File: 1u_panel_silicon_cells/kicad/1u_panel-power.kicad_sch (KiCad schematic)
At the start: 66 parts, among them J1 MMS-104-01-[F/L]-SH, Q1 DMP3050LVT-7, Q2 DMP2240UDM-7, U10 TPS63060DSCR, U12 LTC4412, U3 LT1618EMSTRPBF, U4 INA226AIDGSR

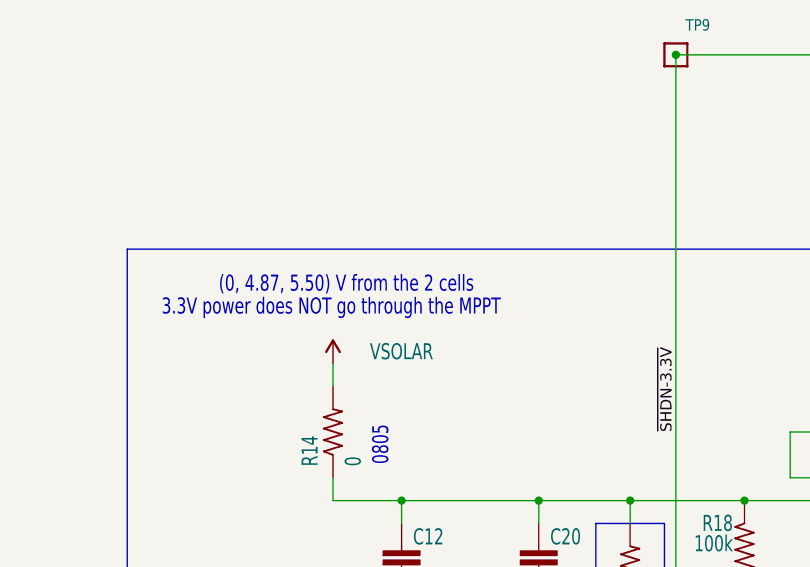
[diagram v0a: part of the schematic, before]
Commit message: fixed board outline, title blocks
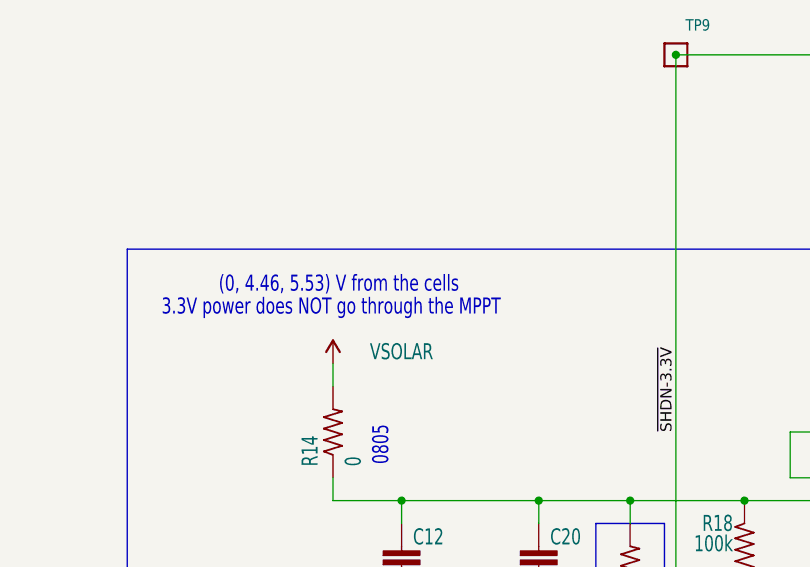
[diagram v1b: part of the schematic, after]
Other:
- note added: "(0, 4.46, 5.53) V from the cells"
- note removed: "(0, 4.87, 5.50) V from the 2 cells"
- title: OreSat Solar Module (for Frame 2.0) -> OreSat Silicon Solar Module (for Frame 2.0)
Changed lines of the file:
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@@
 	(paper "USLedger")
 	(title_block
-		(title "OreSat Solar Module (for Frame 2.0)")
-		(date "2023-12-20")
-		(rev "6.0")
+		(title "OreSat Silicon Solar Module (for Frame 2.0)")
+		(date "2024-08-18")
+		(rev "1.0")
 	)
 	(junction
@@
 		)
 	)
-	(text "(0, 4.87, 5.50) V from the 2 cells"
+	(text "(0, 4.46, 5.53) V from the cells"
 		(exclude_from_sim no)
 		(at 116.84 167.64 0)

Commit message: updating remote repo for design review
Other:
- moved on the sheet: C14
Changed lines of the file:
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@@
 	(wire
 		(pts
-			(xy 162.56 69.85) (xy 162.56 67.31)
+			(xy 162.56 69.85) (xy 162.56 68.58)
 		)
 		(stroke
@@
 	(wire
 		(pts
+			(xy 162.56 60.96) (xy 162.56 59.69)
+		)
+		(stroke
+			(width 0)
+			(type default)
+		)
+	)
+	(wire
+		(pts
 			(xy 91.44 90.17) (xy 93.98 90.17)
 		)
@@
 	(symbol
 		(lib_id "1u_panel-eagle-import:oresat-rcl_C-EU0603-C-NOSILK")
-		(at 162.56 62.23 0)
+		(at 162.56 63.5 0)
 		(unit 1)
 		(exclude_from_sim no)
@@
 		(dnp no)
 		(property "Reference" "C14"
-			(at 164.084 61.849 0)
+			(at 164.084 63.119 0)
 			(effects
 				(font
@@
 		)
 		(property "Value" "4.7u"
-			(at 164.084 66.929 0)
+			(at 164.084 68.199 0)
 			(effects
 				(font
@@
 		)
 		(property "Footprint" "1u_panel:.0603-C-NOSILK"
-			(at 162.56 62.23 0)
+			(at 162.56 63.5 0)
 			(effects
 				(font
@@
 		)
 		(property "Datasheet" ""
-			(at 162.56 62.23 0)
+			(at 162.56 63.5 0)
 			(effects
 				(font
@@
 		)
 		(property "Description" ""
-			(at 162.56 62.23 0)
+			(at 162.56 63.5 0)
 			(effects
 				(font
@@
 		)
 		(property "DIS" "Digi-Key"
-			(at 162.56 62.23 0)
+			(at 162.56 63.5 0)
 			(effects
 				(font
@@
 		)
 		(property "DPN" "587-4332-1-ND"
-			(at 162.56 62.23 0)
+			(at 162.56 63.5 0)
 			(effects
 				(font
@@
 		)
 		(property "MFR" "Taiyo"
-			(at 162.56 62.23 0)
+			(at 162.56 63.5 0)
 			(effects
 				(font
@@
 		)
 		(property "MPN" "EMK107BBJ475KAHT"
-			(at 162.56 62.23 0)
+			(at 162.56 63.5 0)
 			(effects
 				(font

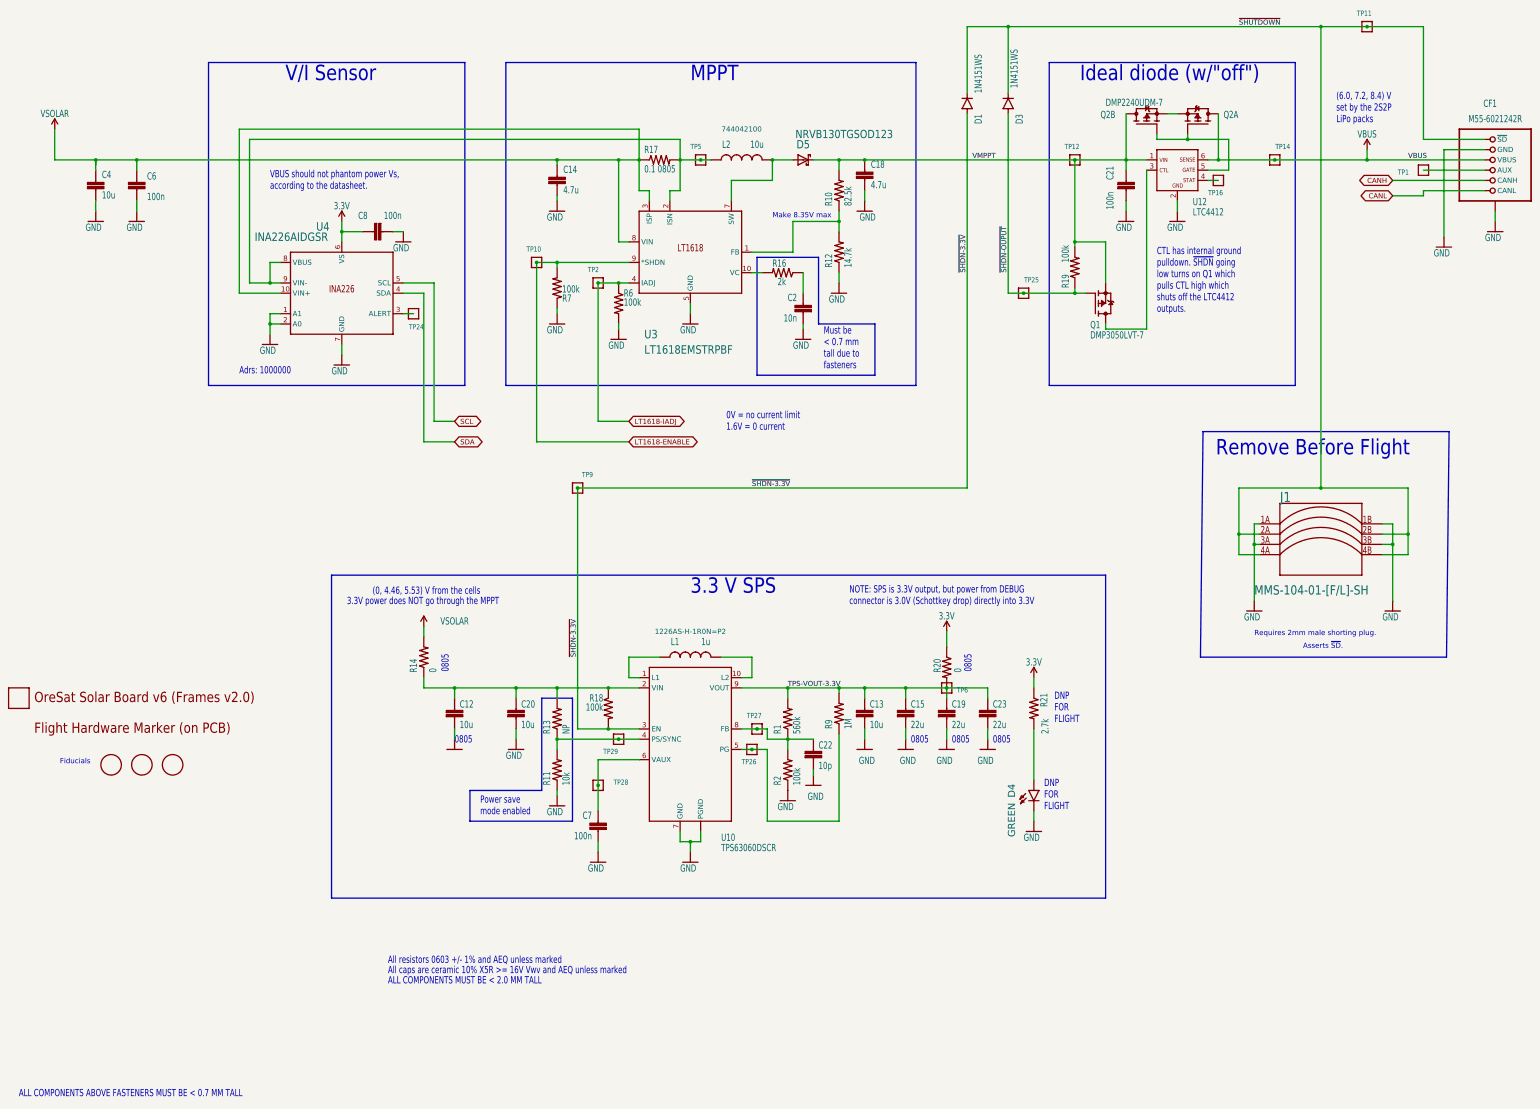
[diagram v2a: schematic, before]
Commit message: commiting silicon solar panel before moving programming header
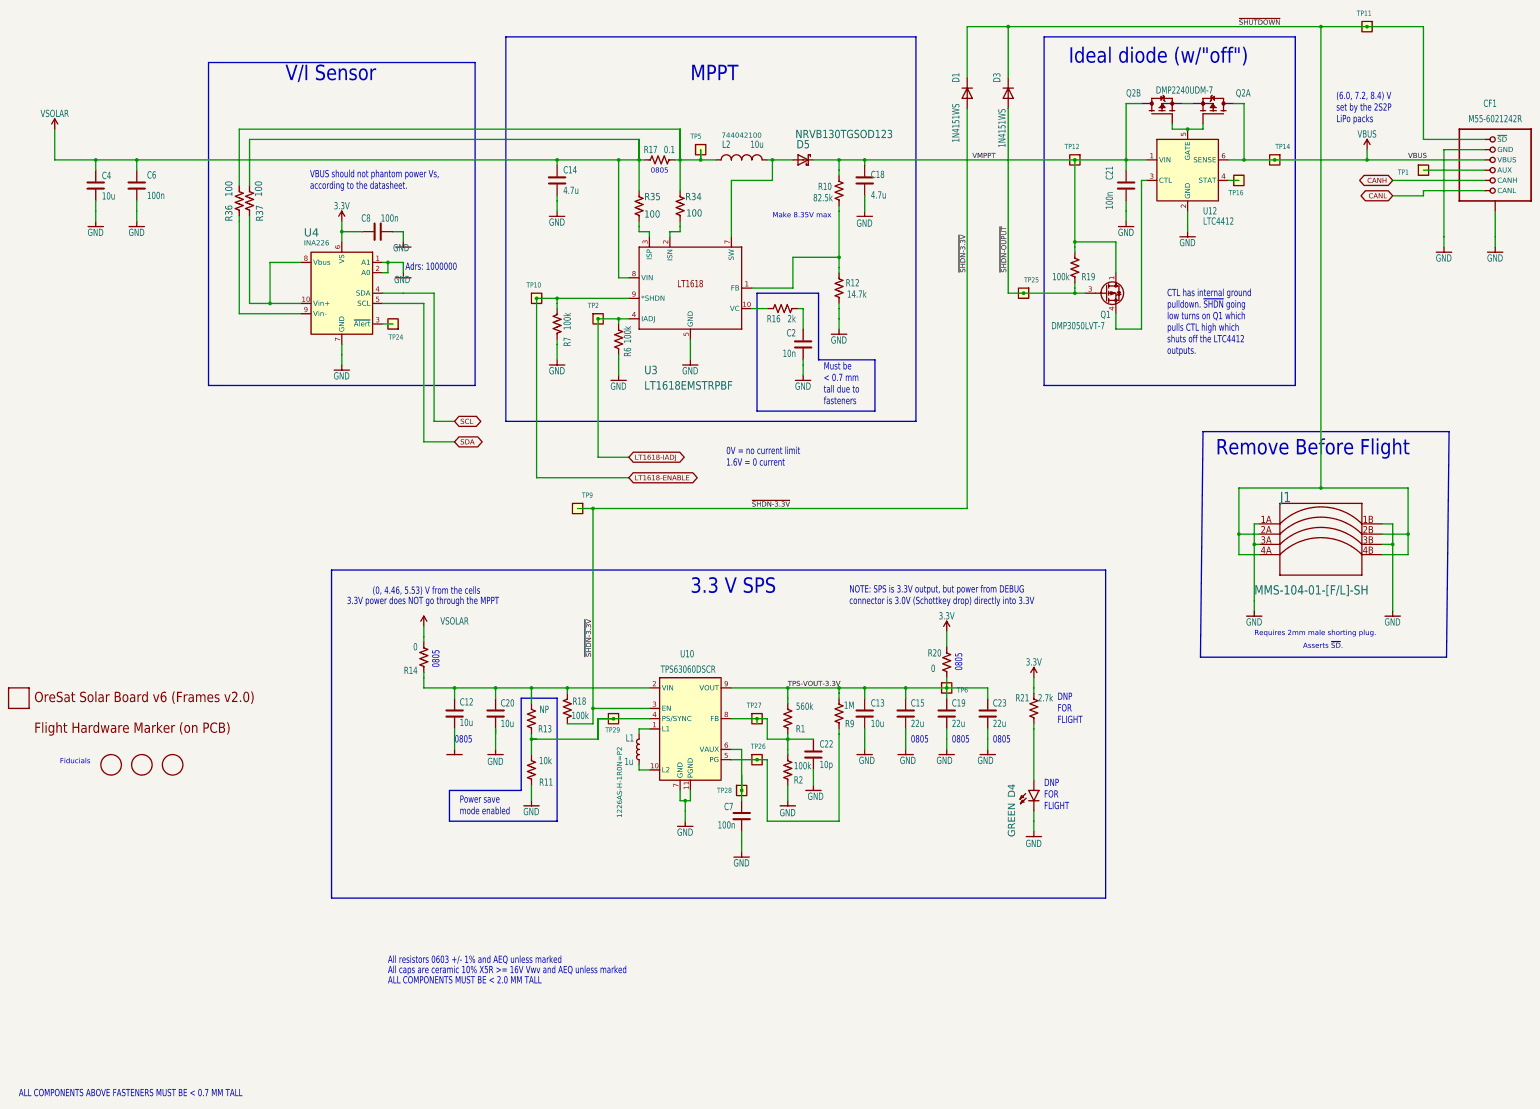
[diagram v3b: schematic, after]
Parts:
- removed U4: INA226AIDGSR, 1u_panel:DGS10, symbol 1u_panel-eagle-import:INA226AIDGSR
- added R34, R35, R36, R37: 100, oresat-passives:0603-C-NOSILK, symbol Device:R_US
- added U4: INA226, Package_SO:VSSOP-10_3x3mm_P0.5mm, symbol Sensor_Energy:INA226
- C12: footprint 1u_panel:.0805-B-NOSILK -> oresat-passives:0805-C-NOSILK; symbol 1u_panel-eagle-import:oresat-rcl_C-EU0805-B-NOSILK -> Device:C; DPN 490-12379-2-ND -> 490-12379-1-ND
- C13, C14, C18, C2, C20, C22, C4, C6, C7, C8: footprint 1u_panel:.0603-C-NOSILK -> oresat-passives:0603-C-NOSILK; symbol 1u_panel-eagle-import:oresat-rcl_C-EU0603-C-NOSILK -> Device:C
- C15, C19, C23: footprint 1u_panel:.0805-B-NOSILK -> oresat-passives:0805-C-NOSILK; symbol 1u_panel-eagle-import:oresat-rcl_C-EU0805-B-NOSILK -> Device:C; DPN 1276-6817-1-ND -> 2571-GMC21X7R226M10NTTR-ND; MFR Samsung -> Cal-Chip; MPN CL32B226KOJVPNE -> GMC21X7R226M10NT
- C21: footprint 1u_panel:.0402-B-NOSILK -> oresat-passives:0603-C-NOSILK; symbol 1u_panel-eagle-import:C-EU0402-B-NOSILK -> Device:C
- CF1: footprint 1u_panel:HARWIN-M55-60X1242R -> oresat-connectors:J-Harwin-M55-60X1242R; symbol 1u_panel-eagle-import:SOLAR-BOARD-CONNECTOR -> oresat-connectors:M55-6021242R; DIS (none) -> Digi-Key; DPN (none) -> 952-3851-2-ND; MFR (none) -> Harwin; MPN (none) -> M55-6021242R
- D1, D3: footprint 1u_panel:SOD323-R -> oresat-diodes:D-SOD323-R; symbol 1u_panel-eagle-import:DIODE-SOD323-R -> Device:D; DIS (none) -> Digi-Key; DPN (none) -> 12-1N4151WS-E3-08TR-ND; MFR (none) -> Vishay; MPN (none) -> 1N4151WS-E3-08
- D4: footprint 1u_panel:LED-0603 -> oresat-diodes:LED-0603
- D5: footprint 1u_panel:SOD123 -> oresat-diodes:SOD123
- J1: footprint 1u_panel:SAMTEC-MMS-104-02-X-SH -> oresat-connectors:SAMTEC-MMS-104-02-X-SH; symbol 1u_panel-eagle-import:SAMTEC-MMS-104-02-X-SHJ -> oresat-connectors:SAMTEC-MMS-104-02-X-SHJ; DIS (none) -> Digi-Key; DPN (none) -> SAM1237-04-ND; MFR (none) -> Samtec; MPN (none) -> MMS-104-02-L-SH
- L1: footprint 1u_panel:IND_1226AS-H-1R0N=P2 -> oresat-passives:IND_1226AS-H-1R0N=P2; symbol 1u_panel-eagle-import:L-MURATA-1226AS-H-1R0N=P2 -> Device:L
- L2: footprint 1u_panel:NONSTANDARD -> oresat-passives:744042100; symbol 1u_panel-eagle-import:L-WURTH-744042100 -> oresat-passives:L_BIG
- PCB1: value ORESAT-SOLAR-BOARD-V4-SPECTROLABS -> ORESAT-SOLAR-BOARD-V1.0-SILICON-CELLS; footprint 1u_panel:ORESAT-SOLAR-BOARD-V4 -> oresat-pcbs:ORESAT-SOLAR-BOARD-V4; MFR (none) -> ORESAT BABAAAYYYYY
- Q1: footprint 1u_panel:SOT23-6 -> Package_TO_SOT_SMD:SOT-23-6; symbol 1u_panel-eagle-import:MOSFET-PCH-SOT23-6 -> oresat-transistors:DMP3050LVT-7
- Q2: footprint 1u_panel:SOT23-6 -> Package_TO_SOT_SMD:SOT-23-6; symbol 1u_panel-eagle-import:Q-MOSFET-PCH-dual-SOT23-6_MOSFET-PCH-SOT23-6 -> oresat-transistors:DMP2240UDM-7
- R1, R10, R13, R16, R18, R19, R2, R21, R6, R7: footprint 1u_panel:.0603-C-NOSILK -> oresat-passives:0603-C-NOSILK; symbol 1u_panel-eagle-import:R-US_0603-C-NOSILK -> Device:R_US
- R11: footprint 1u_panel:.0603-C-NOSILK -> oresat-passives:0603-C-NOSILK; symbol 1u_panel-eagle-import:R-US_0603-C-NOSILK -> Device:R_US; DIS (none) -> Digi-Key; DPN (none) -> RMCF0603JT10K0; MFR (none) -> Stackpole; MPN (none) -> RMCF0603JT10K0
- R12: footprint 1u_panel:.0603-C-NOSILK -> oresat-passives:0603-C-NOSILK; symbol 1u_panel-eagle-import:R-US_0603-C-NOSILK -> Device:R_US; DPN 2019-RN73R1JTTD1422D25CT-ND -> RMCF0603FT14K7TR-ND; MFR KOA -> Stackpole; MPN RN73R1JTTD1422D25 -> RMCF0603FT14K7
- R14, R20: footprint 1u_panel:.0805-C-NOSILK -> oresat-passives:0805-C-NOSILK; symbol 1u_panel-eagle-import:R-US_0805-C-NOSILK -> Device:R_US
- R17: value 0.1 0805 -> 0.1; footprint 1u_panel:.0805-C-NOSILK -> oresat-passives:0805-C-NOSILK; symbol 1u_panel-eagle-import:R-US_0805-C-NOSILK -> Device:R_US; DPN RMCF0805ZT0R00CT-ND -> 541-100MAHTR-ND; MFR Stackpole -> Vishay; MPN RMCF0805ZT0R00 -> CRCW0603100MJPEAHR
- R9: footprint 1u_panel:.0603-C-NOSILK -> oresat-passives:0603-C-NOSILK; symbol 1u_panel-eagle-import:R-US_0603-C-NOSILK -> Device:R_US; DIS (none) -> Digi-Key; DPN (none) -> 311-1.00MHRTR-ND; MFR (none) -> Yaego; MPN (none) -> RC0603FR-071ML
- TP1, TP10, TP11, TP12, TP14, TP16, TP2, TP24, TP25, TP26, TP27, TP28, TP29, TP5, TP6, TP9: footprint 1u_panel:1X01 -> oresat-misc:TestPoint-0.75mm-th; symbol 1u_panel-eagle-import:TEST-POINT-LARGE-SQUARE -> oresat-misc:Test-Point-0.75mm-th; now left out of the parts list
- U$1: footprint 1u_panel:FLIGHTMARKER_NEW_BOARDS -> oresat-graphics:FLIGHTMARKER_NEW_BOARDS
- U$2, U$3, U$4: footprint 1u_panel:FIDUCIAL_1MM -> Fiducial:Fiducial_1mm_Mask2mm
- U10: footprint 1u_panel:CONV_TPS63060DSCT -> Package_SON:Texas_S-PWSON-N10; symbol 1u_panel-eagle-import:U-TI-TPS63060DCT-BUCKBOOST -> Regulator_Switching:TPS63060; DIS (none) -> Digi-Key; DPN (none) -> 296-30204-2-ND; MFR (none) -> Texas Instruments; MPN (none) -> TPS63060DSCR
- U12: footprint 1u_panel:SOT23-6 -> Package_TO_SOT_SMD:TSOT-23-6; symbol 1u_panel-eagle-import:LTC4412 -> Power_Management:LTC4412xS6
- U3: footprint 1u_panel:MSOP-10_MS -> Package_SO:MSOP-10_3x3mm_P0.5mm; symbol 1u_panel-eagle-import:LT1618EMSTRPBF -> oresat-ics:LT1618EMSTRPBF
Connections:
- net 3.3V: now also U4.6 (VS)
- net GND: now also CF1.SH1 (SHIELD), CF1.SH2 (SHIELD), CF1.SH3 (SHIELD), CF1.SH4 (SHIELD), R7.2, U4.1 (A1), U4.2 (A0), U4.7 (GND); no longer CF1.P$1 (SHIELD), CF1.P$2 (SHIELD), CF1.P$3 (SHIELD), CF1.P$4 (SHIELD), R7.1, U10.12 (PGND), U10.13 (PGND), U10.14 (PGND), U10.15 (PGND), U10.16 (PGND), U10.17 (PGND), U10.18 (PGND), U10.19 (PGND)
- net LT1618-ENABLE: now also R7.1; no longer R7.2
- net SCL: now also U4.4 (SDA)
- net SDA: now also U4.5 (SCL)
- net VMPPT: now also Q1.1 (D), Q1.2 (D), Q1.5 (D), Q1.6 (D); no longer Q1.4 (S)
- net VSOLAR: now also R35.2, R37.2; no longer U3.3 (ISP)
- net ~{SHDN-3.3V}: now also D1.2 (A), R18.1; no longer D1.A, R18.2
- net ~{SHDN-OUPUT}: now also D3.2 (A); no longer D3.A
- net ~{SHUTDOWN}: now also D1.1 (K), D3.1 (K); no longer D1.C, D3.C
- net at C12.1, C20.1, R13.2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: now also R18.2; no longer R18.1
- net at L1.1: now also U10.10 (L2); no longer U10.1 (L1)
- net at L1.2: now also U10.1 (L1); no longer U10.10 (L2)
- net at R17.2, TP5.1: now also L2.1, R34.2, R36.2; no longer L2.P$1 (1), U3.2 (ISN)
- net at D5.A (ANODE), U3.7 (SW): now also L2.2; no longer L2.P$2 (2)
- net at TP24.1: now also U4.3 (~{Alert})
- new net: R34.1, U3.2 (ISN)
- new net: R37.1, U4.10 (Vin+), U4.8 (Vbus)
- new net: Q1.4 (S), U12.3 (CTL)
- new net: R35.1, U3.3 (ISP)
- new net: R36.1, U4.9 (Vin-)
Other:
- moved on the sheet: Q2A, Q2B, U3
